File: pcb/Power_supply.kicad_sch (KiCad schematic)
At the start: 31 parts, among them Q1 Si4368DY, SW1 POWER, U1 LTC3872, U2 TLV1117-50, U3 TLV1117-33

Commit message: [pcb] Test point added
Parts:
- added TP1, TP2, TP3, TP4, TP5, TP6: TestPoint, symbol Connector:TestPoint
- R6, R7, R8: value 10.2kR -> ?R
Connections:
- net +3.3V: now also TP6.1
- net +5V: now also TP5.1
- net +BATT: now also TP1.1
- net GND: now also TP3.1, TP4.1
- net at C3.1, C4.1, D1.1 (K)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: now also TP2.1
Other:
- moved on the sheet: C1, C2, C3, C4, C5, C6, C7, D1, F1, L1, Q1, R1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

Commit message: [pcb] Schematic clean-up
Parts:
- added TP3: TestPoint, symbol Connector:TestPoint
- renumbered TP3 to TP4, TP4 to TP5, TP5 to TP6, TP6 to TP7
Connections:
- net GND: now also TP3.1
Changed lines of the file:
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@@
   (junction (at 177.8 33.02) (diameter 0) (color 0 0 0 0)
+  )
+  (junction (at 43.18 44.45) (diameter 0) (color 0 0 0 0)
   )
   (junction (at 99.06 100.33) (diameter 0) (color 0 0 0 0)
@@
     (stroke (width 0) (type default))
   )
+  (wire (pts (xy 43.18 41.91) (xy 43.18 44.45))
+    (stroke (width 0) (type default))
+  )
   (wire (pts (xy 143.51 50.8) (xy 142.24 50.8))
     (stroke (width 0) (type default))
@@
   )
   (wire (pts (xy 99.06 100.33) (xy 99.06 101.6))
+    (stroke (width 0) (type default))
+  )
+  (wire (pts (xy 44.45 41.91) (xy 43.18 41.91))
     (stroke (width 0) (type default))
   )
@@
   (symbol (lib_id "Connector:TestPoint") (at 111.76 90.17 270) (unit 1)
     (in_bom yes) (on_board yes) (dnp no)
-    (property "Reference" "TP6" (at 116.84 90.17 90)
+    (property "Reference" "TP7" (at 116.84 90.17 90)
       (effects (font (size 1.27 1.27)) (justify left))
     )
@@
       (project "Autko"
         (path "/8d5cfdec-de34-4148-9100-7125640c46f5/c078ece0-fea4-45db-aa95-3799eb753f2b"
-          (reference "TP6") (unit 1)
+          (reference "TP7") (unit 1)
         )
       )
@@
     )
   )
+  (symbol (lib_id "Connector:TestPoint") (at 44.45 41.91 270) (unit 1)
+    (in_bom yes) (on_board yes) (dnp no)
+    (property "Reference" "TP3" (at 49.53 41.91 90)
+      (effects (font (size 1.27 1.27)) (justify left))
+    )
+    (property "Value" "TestPoint" (at 45.847 44.45 0)
+      (effects (font (size 1.27 1.27)) (justify left) hide)
+    )
+    (property "Footprint" "" (at 44.45 46.99 0)
+      (effects (font (size 1.27 1.27)) hide)
+    )
+    (property "Datasheet" "~" (at 44.45 46.99 0)
+      (effects (font (size 1.27 1.27)) hide)
+    )
+    (pin "1")
+    (instances
+      (project "Autko"
+        (path "/8d5cfdec-de34-4148-9100-7125640c46f5/c078ece0-fea4-45db-aa95-3799eb753f2b"
+          (reference "TP3") (unit 1)
+        )
+      )
+    )
+  )
   (symbol (lib_id "Connector:TestPoint") (at 44.45 46.99 270) (unit 1)
     (in_bom yes) (on_board yes) (dnp no)
-    (property "Reference" "TP4" (at 49.53 46.99 90)
+    (property "Reference" "TP5" (at 49.53 46.99 90)
       (effects (font (size 1.27 1.27)) (justify left))
     )
@@
       (project "Autko"
         (path "/8d5cfdec-de34-4148-9100-7125640c46f5/c078ece0-fea4-45db-aa95-3799eb753f2b"
-          (reference "TP4") (unit 1)
+          (reference "TP5") (unit 1)
         )
       )
@@
   (symbol (lib_id "Connector:TestPoint") (at 58.42 90.17 270) (unit 1)
     (in_bom yes) (on_board yes) (dnp no)
-    (property "Reference" "TP5" (at 63.5 90.17 90)
+    (property "Reference" "TP6" (at 63.5 90.17 90)
       (effects (font (size 1.27 1.27)) (justify left))
     )
@@
       (project "Autko"
         (path "/8d5cfdec-de34-4148-9100-7125640c46f5/c078ece0-fea4-45db-aa95-3799eb753f2b"
-          (reference "TP5") (unit 1)
+          (reference "TP6") (unit 1)
         )
       )
@@
   (symbol (lib_id "Connector:TestPoint") (at 44.45 44.45 270) (unit 1)
     (in_bom yes) (on_board yes) (dnp no)
-    (property "Reference" "TP3" (at 49.53 44.45 90)
+    (property "Reference" "TP4" (at 49.53 44.45 90)
       (effects (font (size 1.27 1.27)) (justify left))
     )
@@
       (project "Autko"
         (path "/8d5cfdec-de34-4148-9100-7125640c46f5/c078ece0-fea4-45db-aa95-3799eb753f2b"
-          (reference "TP3") (unit 1)
-        )
-      )
+          (reference "TP4") (unit 1)
+        )
+      )

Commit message: [pcb] Footprints assigned
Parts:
- BT1: footprint (none) -> Autko:Keystone_2481RB
- C1, C5, C6, C7: footprint (none) -> Capacitor_SMD:C_0805_2012Metric
- C10, C11, C8, C9: footprint (none) -> Capacitor_Tantalum_SMD:CP_EIA-3216-18_Kemet-A
- C2, C3, C4: footprint (none) -> Capacitor_Tantalum_SMD:CP_EIA-7343-20_Kemet-V
- D1: footprint (none) -> Diode_SMD:D_SOD-123F
- D2, D3, D4: footprint (none) -> LED_SMD:LED_0805_2012Metric
- F1: footprint (none) -> Fuse:Fuse_1812_4532Metric
- L1: footprint (none) -> Inductor_SMD:L_10.4x10.4_H4.8
- R1, R2, R3, R4, R5, R6, R7, R8: footprint (none) -> Resistor_SMD:R_0805_2012Metric
- TP1, TP2, TP6, TP7: footprint (none) -> TestPoint:TestPoint_Pad_D2.0mm
- TP3, TP4, TP5: footprint (none) -> TestPoint:TestPoint_Keystone_5019_Minature
- U1: footprint (none) -> Package_TO_SOT_SMD:SOT-223-8
- U2, U3: footprint (none) -> Package_TO_SOT_SMD:SOT-223-3_TabPin2
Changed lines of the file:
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@@
       (effects (font (size 1.27 1.27)) (justify right))
     )
-    (property "Footprint" "" (at 127 41.91 0)
+    (property "Footprint" "Package_TO_SOT_SMD:SOT-223-8" (at 127 41.91 0)
       (effects (font (size 1.27 1.27)) hide)
     )
@@
       (effects (font (size 1.27 1.27)))
     )
-    (property "Footprint" "" (at 99.06 46.482 90)
+    (property "Footprint" "Resistor_SMD:R_0805_2012Metric" (at 99.06 46.482 90)
       (effects (font (size 1.27 1.27)) hide)
     )
@@
       (effects (font (size 1.27 1.27)) (justify left))
     )
-    (property "Footprint" "" (at 80.9752 54.61 0)
+    (property "Footprint" "Capacitor_SMD:C_0805_2012Metric" (at 80.9752 54.61 0)
       (effects (font (size 1.27 1.27)) hide)
     )
@@
       (effects (font (size 1.27 1.27)))
     )
-    (property "Footprint" "" (at 45.72 90.17 0)
+    (property "Footprint" "Package_TO_SOT_SMD:SOT-223-3_TabPin2" (at 45.72 90.17 0)
       (effects (font (size 1.27 1.27)) hide)
     )
@@
       (effects (font (size 1.27 1.27)) (justify left))
     )
-    (property "Footprint" "" (at 184.912 43.18 90)
+    (property "Footprint" "Resistor_SMD:R_0805_2012Metric" (at 184.912 43.18 90)
       (effects (font (size 1.27 1.27)) hide)
     )
@@
       (effects (font (size 1.27 1.27)) (justify left) hide)
     )
-    (property "Footprint" "" (at 191.77 31.75 0)
+    (property "Footprint" "TestPoint:TestPoint_Pad_D2.0mm" (at 191.77 31.75 0)
       (effects (font (size 1.27 1.27)) hide)
     )
@@
       (effects (font (size 1.27 1.27)) (justify right))
     )
-    (property "Footprint" "" (at 58.42 138.43 0)
+    (property "Footprint" "LED_SMD:LED_0805_2012Metric" (at 58.42 138.43 0)
       (effects (font (size 1.27 1.27)) hide)
     )
@@
       (effects (font (size 1.27 1.27)) (justify left) hide)
     )
-    (property "Footprint" "" (at 111.76 95.25 0)
+    (property "Footprint" "TestPoint:TestPoint_Pad_D2.0mm" (at 111.76 95.25 0)
       (effects (font (size 1.27 1.27)) hide)
     )
@@
       (effects (font (size 1.27 1.27)) (justify left))
     )
-    (property "Footprint" "" (at 58.1152 99.06 0)
+    (property "Footprint" "Capacitor_Tantalum_SMD:CP_EIA-3216-18_Kemet-A" (at 58.1152 99.06 0)
       (effects (font (size 1.27 1.27)) hide)
     )
@@
       (effects (font (size 1.27 1.27)) (justify left))
     )
-    (property "Footprint" "" (at 106.3752 60.96 0)
+    (property "Footprint" "Capacitor_SMD:C_0805_2012Metric" (at 106.3752 60.96 0)
       (effects (font (size 1.27 1.27)) hide)
     )
@@
       (effects (font (size 1.27 1.27)) (justify left))
     )
-    (property "Footprint" "" (at 184.912 53.34 90)
+    (property "Footprint" "Resistor_SMD:R_0805_2012Metric" (at 184.912 53.34 90)
       (effects (font (size 1.27 1.27)) hide)
     )
@@
       (effects (font (size 1.27 1.27)) (justify left))
     )
-    (property "Footprint" "" (at 43.942 129.54 90)
+    (property "Footprint" "Resistor_SMD:R_0805_2012Metric" (at 43.942 129.54 90)
       (effects (font (size 1.27 1.27)) hide)
     )
@@
       (effects (font (size 1.27 1.27)) (justify left))
     )
-    (property "Footprint" "" (at 93.6752 60.96 0)
+    (property "Footprint" "Capacitor_SMD:C_0805_2012Metric" (at 93.6752 60.96 0)
       (effects (font (size 1.27 1.27)) hide)
     )
@@
       (effects (font (size 1.27 1.27)) (justify left))
     )
-    (property "Footprint" "" (at 27.94 39.116 90)
+    (property "Footprint" "Autko:Keystone_2481RB" (at 27.94 39.116 90)
       (effects (font (size 1.27 1.27)) hide)
     )
@@
       (effects (font (size 1.27 1.27)) (justify right))
     )
-    (property "Footprint" "" (at 45.72 138.43 0)
+    (property "Footprint" "LED_SMD:LED_0805_2012Metric" (at 45.72 138.43 0)
       (effects (font (size 1.27 1.27)) hide)
     )
@@
       (effects (font (size 1.27 1.27)) (justify left))
     )
-    (property "Footprint" "" (at 111.4552 99.06 0)
+    (property "Footprint" "Capacitor_Tantalum_SMD:CP_EIA-3216-18_Kemet-A" (at 111.4552 99.06 0)
       (effects (font (size 1.27 1.27)) hide)
     )
@@
       (effects (font (size 1.27 1.27)) (justify left))
     )
-    (property "Footprint" "" (at 33.3248 99.06 0)
+    (property "Footprint" "Capacitor_Tantalum_SMD:CP_EIA-3216-18_Kemet-A" (at 33.3248 99.06 0)
       (effects (font (size 1.27 1.27)) hide)
     )
@@
       (effects (font (size 1.27 1.27)) (justify left) hide)
     )
-    (property "Footprint" "" (at 44.45 46.99 0)
+    (property "Footprint" "TestPoint:TestPoint_Keystone_5019_Minature" (at 44.45 46.99 0)
       (effects (font (size 1.27 1.27)) hide)
     )
@@
       (effects (font (size 1.27 1.27)) (justify left) hide)
     )
-    (property "Footprint" "" (at 44.45 52.07 0)
+    (property "Footprint" "TestPoint:TestPoint_Keystone_5019_Minature" (at 44.45 52.07 0)
       (effects (font (size 1.27 1.27)) hide)
     )
@@
       (effects (font (size 1.27 1.27)) (justify left))
     )
-    (property "Footprint" "" (at 78.232 40.64 90)
+    (property "Footprint" "Resistor_SMD:R_0805_2012Metric" (at 78.232 40.64 90)
       (effects (font (size 1.27 1.27)) hide)
     )
@@
       (effects (font (size 1.27 1.27)) (justify left) hide)
     )
-    (property "Footprint" "" (at 58.42 95.25 0)
+    (property "Footprint" "TestPoint:TestPoint_Pad_D2.0mm" (at 58.42 95.25 0)
       (effects (font (size 1.27 1.27)) hide)
     )
@@
       (effects (font (size 1.27 1.27)) (justify left))
     )
-    (property "Footprint" "" (at 86.6648 99.06 0)
+    (property "Footprint" "Capacitor_Tantalum_SMD:CP_EIA-3216-18_Kemet-A" (at 86.6648 99.06 0)
       (effects (font (size 1.27 1.27)) hide)
     )
@@
       (effects (font (size 1.27 1.27)))
     )
-    (property "Footprint" "" (at 160.02 33.02 0)
+    (property "Footprint" "Diode_SMD:D_SOD-123F" (at 160.02 33.02 0)
       (effects (font (size 1.27 1.27)) hide)
     )
@@
       (effects (font (size 1.27 1.27)) (justify left))
     )
-    (property "Footprint" "" (at 178.7652 41.91 0)
+    (property "Footprint" "Capacitor_Tantalum_SMD:CP_EIA-7343-20_Kemet-V" (at 178.7652 41.91 0)
       (effects (font (size 1.27 1.27)) hide)
     )
@@
       (effects (font (size 1.27 1.27)) (justify left))
     )
-    (property "Footprint" "" (at 69.5452 41.91 0)
+    (property "Footprint" "Capacitor_Tantalum_SMD:CP_EIA-7343-20_Kemet-V" (at 69.5452 41.91 0)
       (effects (font (size 1.27 1.27)) hide)
     )
@@
       (effects (font (size 1.27 1.27)) (justify right))
     )
-    (property "Footprint" "" (at 33.02 138.43 0)
+    (property "Footprint" "LED_SMD:LED_0805_2012Metric" (at 33.02 138.43 0)
       (effects (font (size 1.27 1.27)) hide)
     )
@@
       (effects (font (size 1.27 1.27)) (justify left))
     )
-    (property "Footprint" "" (at 56.642 129.54 90)
+    (property "Footprint" "Resistor_SMD:R_0805_2012Metric" (at 56.642 129.54 90)
       (effects (font (size 1.27 1.27)) hide)
     )
@@
       (effects (font (size 1.27 1.27)))
     )
-    (property "Footprint" "" (at 196.85 31.75 0)
+    (property "Footprint" "Fuse:Fuse_1812_4532Metric" (at 196.85 31.75 0)
       (effects (font (size 1.27 1.27)) (justify left) hide)
     )
@@
       (effects (font (size 1.27 1.27)))
     )
-    (property "Footprint" "" (at 109.22 37.7952 0)
+    (property "Footprint" "Capacitor_SMD:C_0805_2012Metric" (at 109.22 37.7952 0)
       (effects (font (size 1.27 1.27)) hide)
     )
@@
       (effects (font (size 1.27 1.27)) (justify left))
     )
-    (property "Footprint" "" (at 168.6052 41.91 0)
+    (property "Footprint" "Capacitor_Tantalum_SMD:CP_EIA-7343-20_Kemet-V" (at 168.6052 41.91 0)
       (effects (font (size 1.27 1.27)) hide)
     )
@@
       (effects (font (size 1.27 1.27)) (justify left))
     )
-    (property "Footprint" "" (at 150.622 54.61 90)
+    (property "Footprint" "Resistor_SMD:R_0805_2012Metric" (at 150.622 54.61 90)
       (effects (font (size 1.27 1.27)) hide)
     )
@@
       (effects (font (size 1.27 1.27)) (justify left))
     )
-    (property "Footprint" "" (at 31.242 129.54 90)
+    (property "Footprint" "Resistor_SMD:R_0805_2012Metric" (at 31.242 129.54 90)
       (effects (font (size 1.27 1.27)) hide)
     )
@@
       (effects (font (size 1.27 1.27)) (justify left) hide)
     )
-    (property "Footprint" "" (at 44.45 49.53 0)
+    (property "Footprint" "TestPoint:TestPoint_Keystone_5019_Minature" (at 44.45 49.53 0)
       (effects (font (size 1.27 1.27)) hide)
     )
@@
       (effects (font (size 1.27 1.27)) (justify left) hide)
     )
-    (property "Footprint" "" (at 44.45 36.83 0)
+    (property "Footprint" "TestPoint:TestPoint_Pad_D2.0mm" (at 44.45 36.83 0)
       (effects (font (size 1.27 1.27)) hide)
     )
@@
       (effects (font (size 1.27 1.27)))
     )
-    (property "Footprint" "" (at 130.81 33.02 0)
+    (property "Footprint" "Inductor_SMD:L_10.4x10.4_H4.8" (at 130.81 33.02 0)
       (effects (font (size 1.27 1.27)) hide)
     )
@@
       (effects (font (size 1.27 1.27)))
     )
-    (property "Footprint" "" (at 99.06 90.17 0)
-      (effects (font (size 1.27 1.27)) hide)
-    )
+    (property "Footprint" "Package_TO_SOT_SMD:SOT-223-3_TabPin2" (at 99.06 90.17 0)
+      (effects (font (size 1.27 1.27)) hide)
+    )

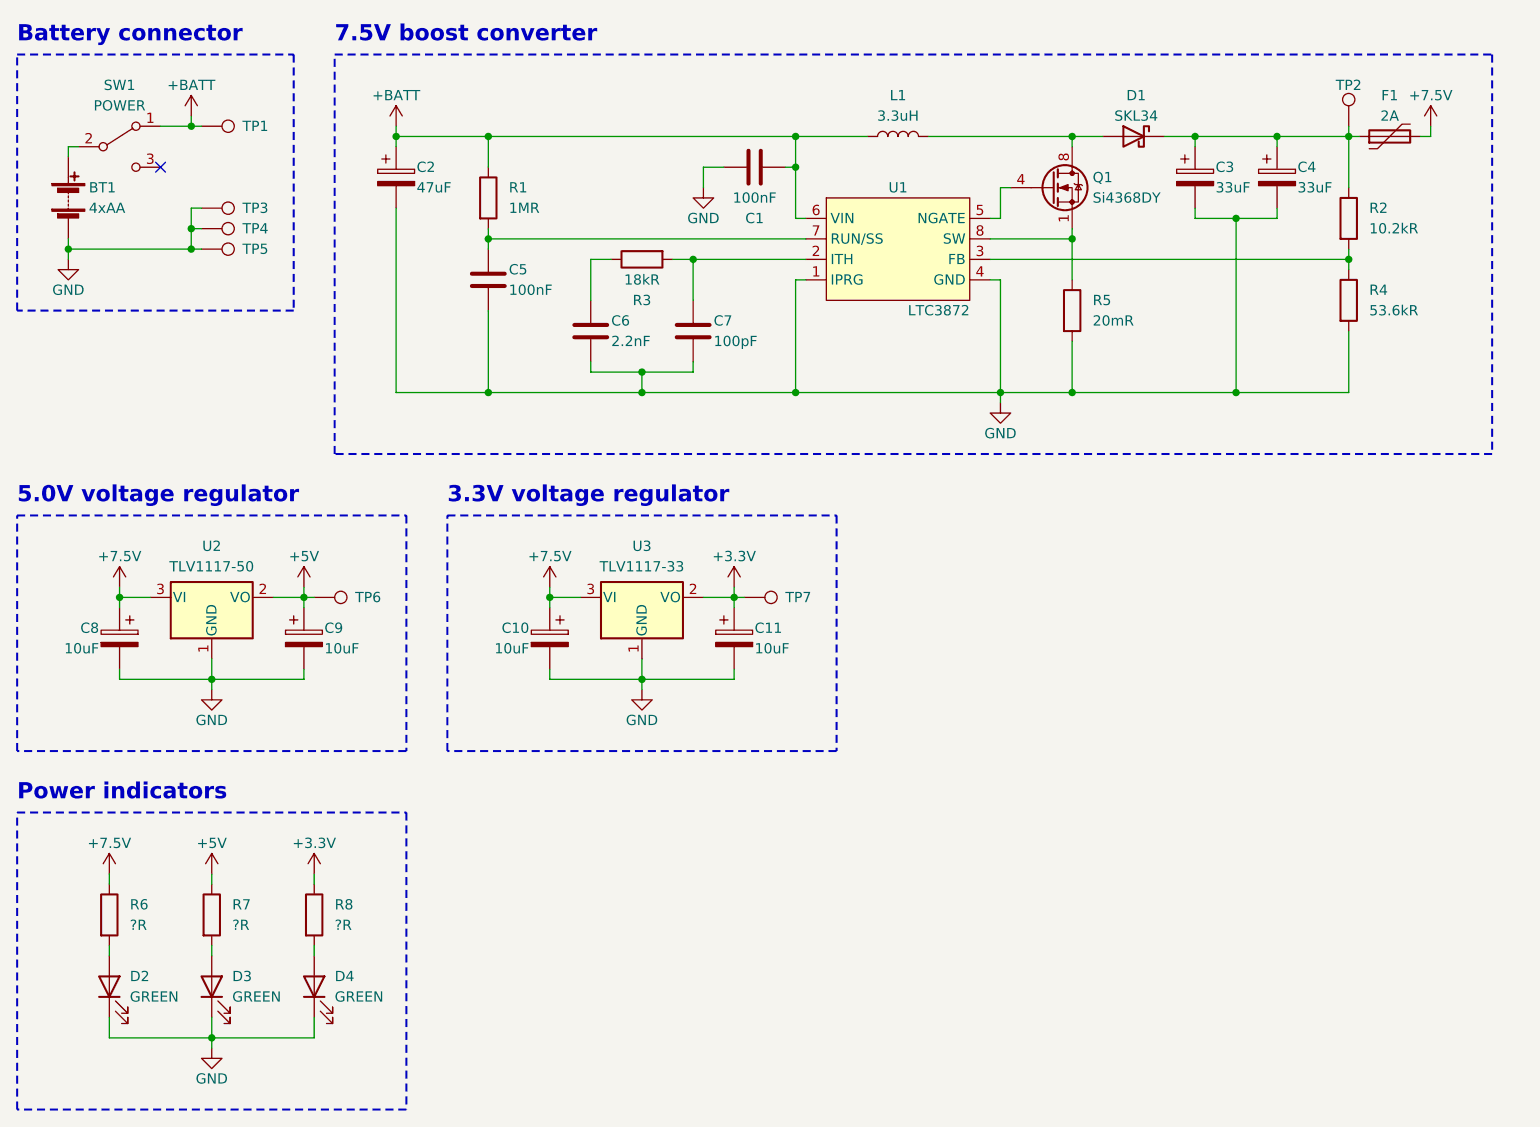
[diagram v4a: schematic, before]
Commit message: [pcb] Rework schematic for ATxmega16A4U
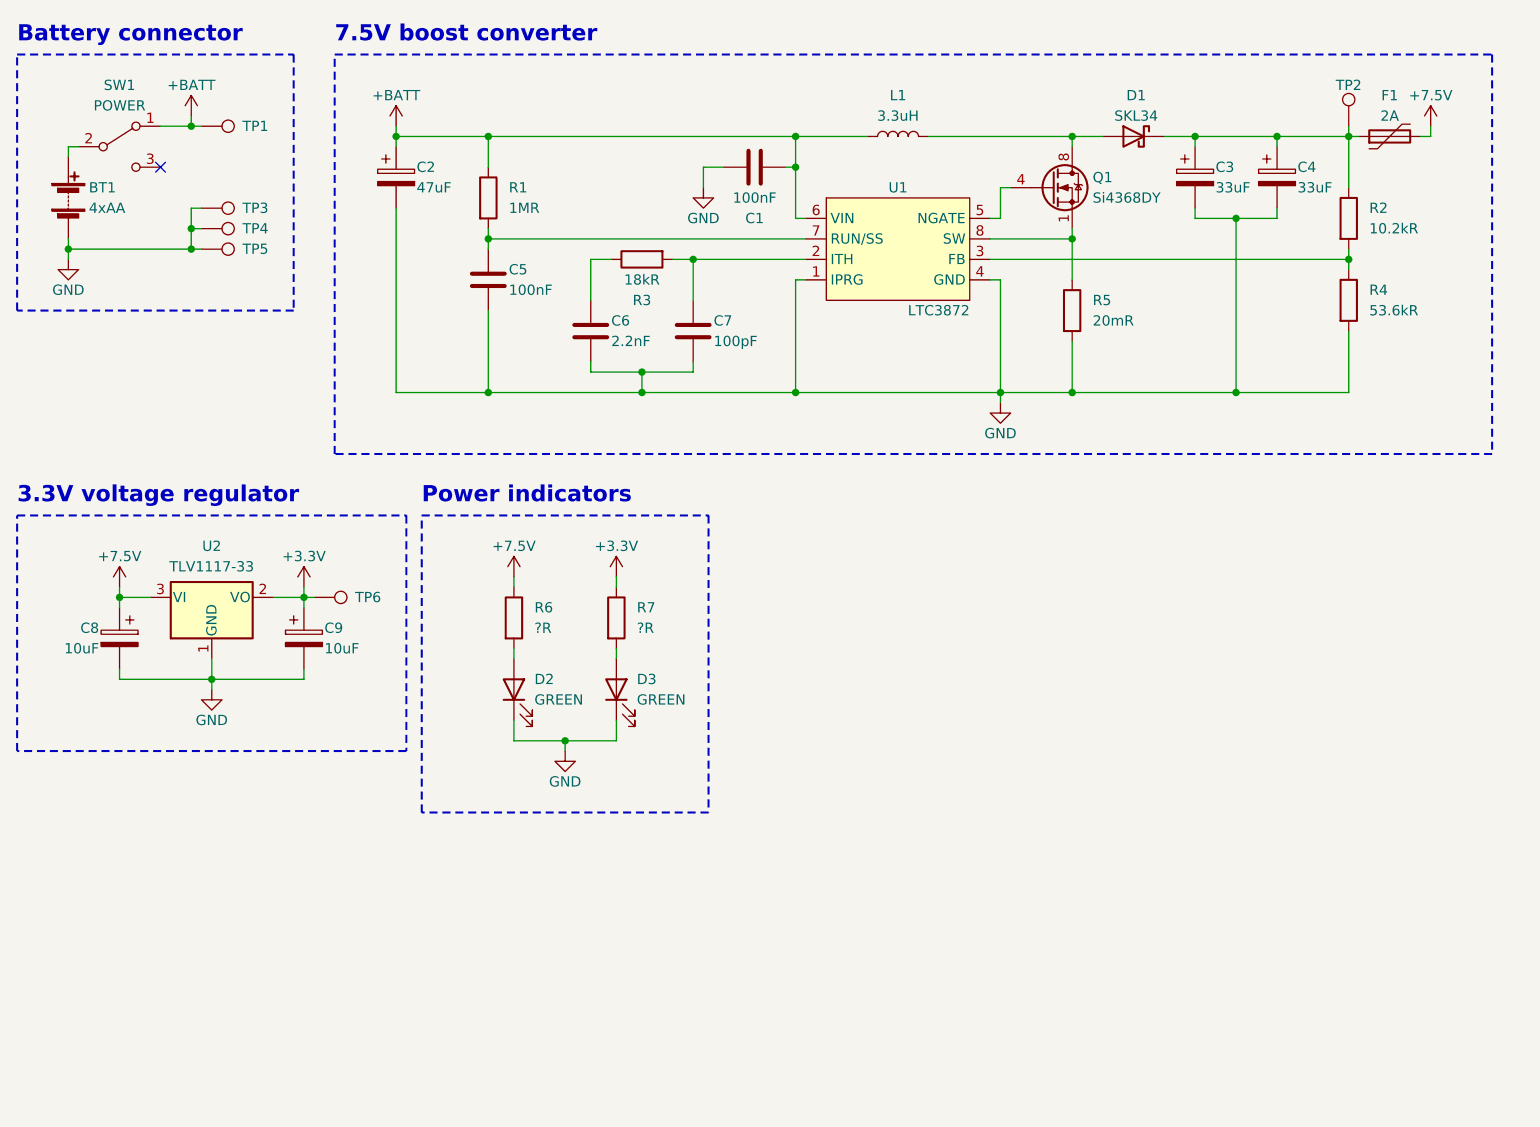
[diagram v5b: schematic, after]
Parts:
- removed C10, C11: 10uF, Capacitor_Tantalum_SMD:CP_EIA-3216-18_Kemet-A, symbol Device:C_Polarized
- removed D4: GREEN, LED_SMD:LED_0805_2012Metric, symbol Device:LED
- removed R8: ?R, Resistor_SMD:R_0805_2012Metric, symbol Device:R
- removed TP7: TestPoint, TestPoint:TestPoint_Pad_D2.0mm, symbol Connector:TestPoint
- removed U2: TLV1117-50, Package_TO_SOT_SMD:SOT-223-3_TabPin2, symbol Regulator_Linear:TLV1117-50
- renumbered U3 to U2
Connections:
- net +5V is gone; now on net +3.3V: C9.1, R7.1, TP6.1
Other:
- note removed: "5.0V voltage regulator"
- moved on the sheet: D2, D3, R6, R7, U2

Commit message: [pcb] Power switch footprint assigned
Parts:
- SW1: footprint (none) -> Autko:Knitter-Switch_MSS_3112_D
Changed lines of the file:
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@@
       (effects (font (size 1.27 1.27)))
     )
-    (property "Footprint" "" (at 34.29 34.29 0)
+    (property "Footprint" "Autko:Knitter-Switch_MSS_3112_D" (at 34.29 34.29 0)
       (effects (font (size 1.27 1.27)) hide)
     )

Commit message: [pcb] Boost converter routing
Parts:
- U1: footprint Package_TO_SOT_SMD:SOT-223-8 -> Package_TO_SOT_SMD:SOT-23-8
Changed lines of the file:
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@@
       (effects (font (size 1.27 1.27)) (justify right))
     )
-    (property "Footprint" "Package_TO_SOT_SMD:SOT-223-8" (at 127 41.91 0)
+    (property "Footprint" "Package_TO_SOT_SMD:SOT-23-8" (at 127 41.91 0)
       (effects (font (size 1.27 1.27)) hide)
     )

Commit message: [pcb] Some power routing
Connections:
- net +3.3V: now also D3.2 (A); no longer R7.1
- net +7.5V: now also D2.2 (A), TP2.1; no longer R6.1
- net GND: now also R6.2, R7.2; no longer D2.1 (K), D3.1 (K)
- net at C3.1, C4.1, D1.1 (K)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: no longer TP2.1
- new net: D3.1 (K), R7.1
- new net: D2.1 (K), R6.1
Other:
- moved on the sheet: D2, D3, R6, R7, TP2
